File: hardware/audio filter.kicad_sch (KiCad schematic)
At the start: 59 parts, among them J1 721A, J11 Conn_01x09_Pin, J2 35RAPC2AV, J3 35RAPC2AV, J4 35RAPC4BV4, J5 35RAPC2AV, J6 35RAPC4BV4, J7 BPJF04AUX, J8 Conn_01x03_Pin, J9 Conn_01x02_Pin, K1 K1C05, SW2 SW-T2-1C-A-A2-M1, SW3 SW-T2-1C-A-A2-M1, SW4 SW-T2-1C-A-A2-M1, SW5 SW-T2-1C-A-A2-M1, SW6 SW-T2-1C-A-A2-M1, U5 LM4040LP-3

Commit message: Version 0.3 RE-arranged circuit into external connections and on-board headers. Changed FBs to 10uH inductors.
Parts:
- removed FB1, FB2, FB3, FB4, FB5, FB6: FerriteBead, symbol Device:FerriteBead
- removed J11: Conn_01x09_Pin, symbol Connector:Conn_01x09_Pin
- removed J8: Conn_01x03_Pin, symbol Connector:Conn_01x03_Pin
- removed TP1, TP13, TP2, TP3, TP4, TP5: TestPoint, symbol Connector:TestPoint
- added D2: LED, symbol Device:LED
- added J1: Conn_01x13_Pin, symbol Connector:Conn_01x13_Pin
- added J1, J11, J12, J13, J16, J17, J19, J3, J8, J9: Conn_01x01_Socket, symbol Connector:Conn_01x01_Socket
- added J10, J11, J12, J3, J4, J5, J6, J7, J8: Conn_01x02_Pin, symbol Connector:Conn_01x02_Pin
- added J10, J14, J15, J18, J20, J21, J22, J23: Conn_01x02_Socket, symbol Connector:Conn_01x02_Socket
- added J2: Conn_01x04_Pin, symbol Connector:Conn_01x04_Pin
- added L1, L2, L3, L4, L5, L6: 10u, symbol Device:L
- added R1: 470, symbol Device:R
- renumbered J4 to J13, J3 to J14, J5 to J15, J1 to J16, J6 to J17, J7 to J18, SW6 to SW1
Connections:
- net +5V: now also R1.1
- net 3V3: no longer A5.9 (A1), RV2.2
- net DASH: now also J1.12 (Pin_12); no longer C5.1
- net DOT: now also J1.11 (Pin_11); no longer C6.1
- net GND: now also J1.13 (Pin_13), J1.3 (Pin_3), J1.8 (Pin_8), J10.2 (Pin_2), J12.2 (Pin_2), J3.1 (Pin_1), J3.2 (Pin_2), J5.1 (Pin_1), J6.1 (Pin_1), J7.2 (Pin_2); no longer C3.2, C4.2, C5.2, C6.2, C7.2, D4.1 (K), J13.G, J13.S, J14.S, J15.S, J17.G, J17.R, J17.S, J2.S, J2.TN, J9.2 (Pin_2), SW2.1 (A), SW3.1 (A), SW4.1 (A), SW5.1 (A)
- net GNDA: now also J4.1 (Pin_1)
- net KEY_IN: now also J1.10 (Pin_10); no longer C4.1
- net KEY_OUT: now also J2.1 (Pin_1)
- net at D1.2 (A), K1.8, TR2.1 (C): now also J11.2 (Pin_2)
- net at R6.2, TR1.2 (B): now also J5.2 (Pin_2); no longer J17.RN
- net at C1.2, C8.1, R5.1: now also J7.1 (Pin_1); no longer C3.1, J9.1 (Pin_1)
- net at D4.2 (A): now also J23.1 (Pin_1); no longer R8.2
- net at J13.R: now also L4.1
- net at J13.T: now also L5.1
- net AUDIO_IN: now reaches A2.31 (GPIO26_ADC0), C1.1, R3.2, R4.1
- net at SW1.2 (B): now also J20.1 (Pin_1); no longer A1.8 (VIN+)
- net GNDPWR: now reaches C2.2, J16.2
- net GNDPWR: now also C3.2, C4.2, C5.2, C6.2, C7.2, J13.G, J13.S, J14.S, J15.S, J17.G, J17.R, J17.S, J2.S, J2.TN, J10.2 (Pin_2), J14.1 (Pin_1), J20.2 (Pin_2), J21.2 (Pin_2), J22.1 (Pin_1), J3.1 (Pin_1); no longer A1.9 (VIN-)
- net at C2.1, SW1.1 (A): now also L2.2
- net \FC_BW_MODE: now reaches A2.4 (GPIO2), JP1.2 (B)
- net \FC_BW_MODE: now also J1.4 (Pin_4)
- net at SW2.2 (B): now also J1.1 (Pin_1); no longer A2.6 (GPIO4)
- net at A3.7 (LOUT): now also J10.1 (Pin_1); no longer J17.T
- net at J17.TN: now also J22.2 (Pin_2); no longer A4.5 (A+)
- net at C7.1: now also J14.2 (Pin_2), L6.2; no longer K1.6
- net at J2.T: now also L1.1
- net at J18.1 (In): now also J18.1 (Pin_1); no longer A4.7 (Vout+)
- net at J18.2 (Ext): now also J18.2 (Pin_2); no longer A4.6 (Vout-)
- net at SW3.2 (B): now also J8.1 (Pin_1); no longer A2.7 (GPIO5)
- net at BT1.1 (+), J16.1: now also L2.1
- net at J15.T: now also L6.1
- net UART0_TX: now reaches A2.1 (GPIO0)
- net UART0_TX: now also J1.1 (Pin_1)
- net UART0_RX: now reaches A2.2 (GPIO1)
- net UART0_RX: now also J1.2 (Pin_2)
- net SPARE0: now reaches A2.5 (GPIO3)
- net SPARE0: now also J1.5 (Pin_5)
- net at SW4.2 (B): now also J9.1 (Pin_1); no longer A2.9 (GPIO6)
- net at J14.T: now also L3.1
- net LED1 renamed SPARE1
- net SPARE1: now also J2.3 (Pin_3)
- net LED2 renamed SPARE2
- net SPARE2: now also J2.4 (Pin_4)
- net TUNE: no longer names the net of SW5.2 (B)
- net TUNE: now also J11.1 (Pin_1); no longer A2.15 (GPIO11)
- new net: C5.1, J17.1 (Pin_1), L4.2
- new net: C4.1, J13.1 (Pin_1), L3.2
- new net: D4.1 (K), J23.2 (Pin_2)
- new net: J12.1 (Pin_1), R8.2
- new net: A5.9 (A1), RV2.2
- new net: A1.8 (VIN+), J9.1 (Pin_1)
- new net: A1.9 (VIN-), J9.2 (Pin_2)
- new net: J12.1 (Pin_1), SW2.1 (A), SW3.1 (A), SW4.1 (A), SW5.1 (A)
- new net: J17.RN, J17.T, J19.1 (Pin_1), J21.1 (Pin_1)
- new net: J11.1 (Pin_1), R1.2
- new net: J6.2 (Pin_2), K1.6
- new net: D2.1 (K), J15.2 (Pin_2)
- new net: D2.2 (A), J15.1 (Pin_1)
- new net: C3.1, J10.1 (Pin_1), L1.2
- new net: A4.7 (Vout+), J8.1 (Pin_1)
- new net: A4.6 (Vout-), J8.2 (Pin_2)
- new net: C6.1, J16.1 (Pin_1), L5.2
- new net: A4.5 (A+), J4.2 (Pin_2)
- new net \ALE_IN: A2.7 (GPIO5), J1.7 (Pin_7)
- new net \AN: A2.9 (GPIO6), J1.9 (Pin_9)
- new net \FILTER_IN: A2.6 (GPIO4), J1.6 (Pin_6)
- new net \TUNE: A2.15 (GPIO11), J2.2 (Pin_2)
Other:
- note added: "1 S"
- note added: "2 T"
- note added: "3 RN"
- note added: "35RAPC4BV4"
- note added: "4 R"
- note added: "5 TN"
- note added: "G"
- note added: "Isolate from Ground"
- note added: "TUNE LED RED, 3mm"
- note removed: "Debugger"
- moved on the sheet: A1, A2, A3, A4, A5, BT1, C1, D1, D4, J13, J14, J15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

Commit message: Revision A (Prototype).
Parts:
- removed J19: Conn_01x01_Socket, symbol Connector:Conn_01x01_Socket
- removed J2: Conn_01x04_Pin, symbol Connector:Conn_01x04_Pin
- added PL2: Conn_01x04_Pin, symbol Connector:Conn_01x04_Pin
- added SK5: Conn_01x02_Socket, symbol Connector:Conn_01x02_Socket
- renumbered J13 to J1, J14 to J2, J15 to J3, J2 to J4, J16 to J5, J17 to J6, J18 to J7, J1 to PL1, J10 to PL10, J11 to PL11, J12 to PL12, J3 to PL3, J4 to PL4, J5 to PL5, J6 to PL6, J7 to PL7, J8 to PL8, J9 to PL9, J21 to SK10, J15 to SK11, J23 to SK12, J1 to SK1a1, J8 to SK1b1, J12 to SK1c1, J9 to SK1d1, J13 to SK1e1, J16 to SK1f1, J17 to SK1g1, J3 to SK1h1, J11 to SK2a1, J22 to SK4, J14 to SK6, J10 to SK7, J18 to SK8, J20 to SK9
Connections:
- net KEY_OUT: now also PL2.1 (Pin_1)
- net SPARE1: now also PL2.3 (Pin_3)
- net SPARE2: now also PL2.4 (Pin_4)
- net \TUNE: now also PL2.2 (Pin_2)
- net at J6.RN, J6.T, SK10.1 (Pin_1): now also SK5.2 (Pin_2)

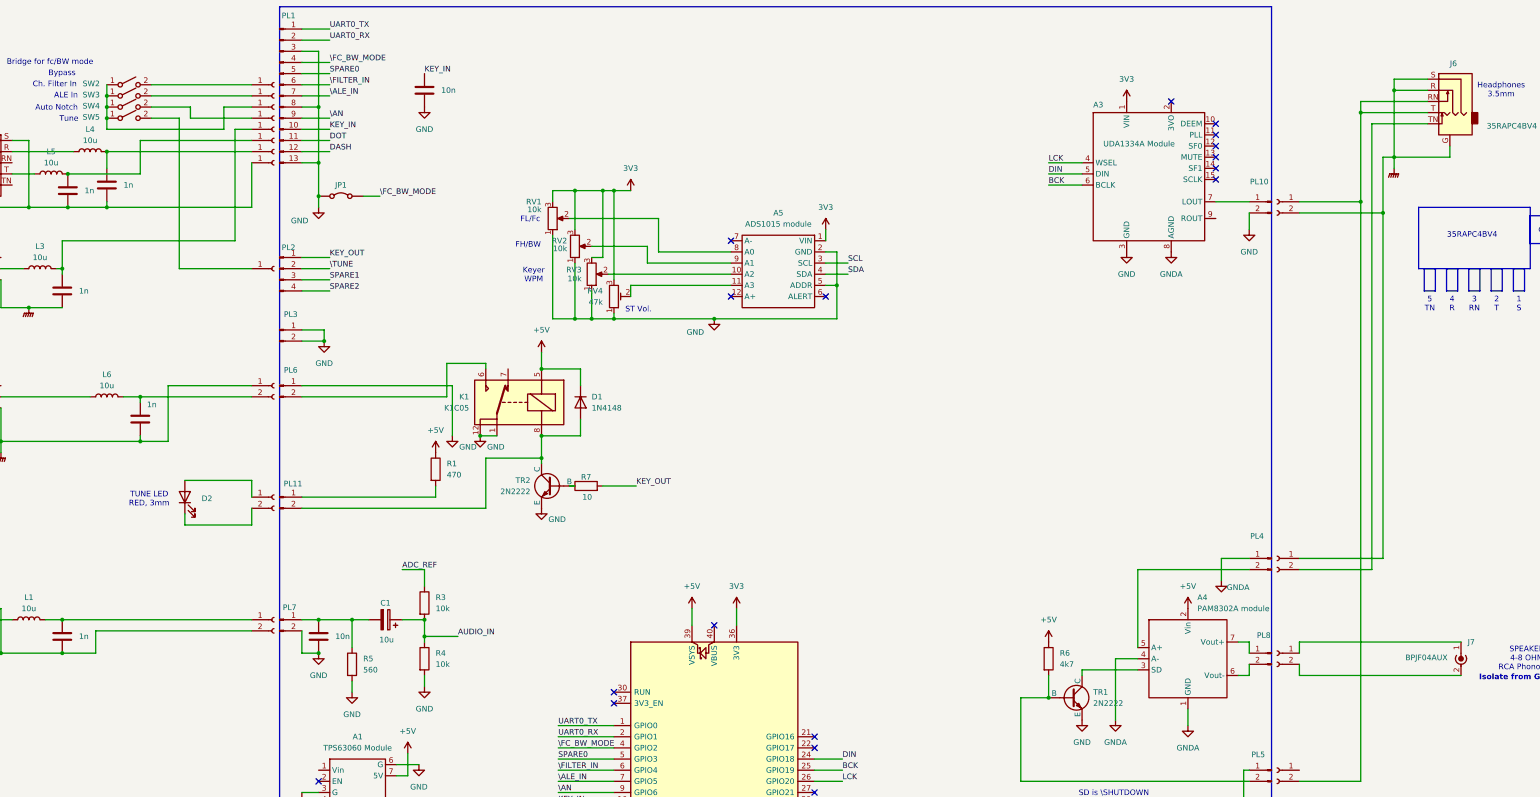
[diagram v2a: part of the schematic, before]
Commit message: Added 1n C10/C11 to SPKR output to filter out RF. Started modle footprint library.
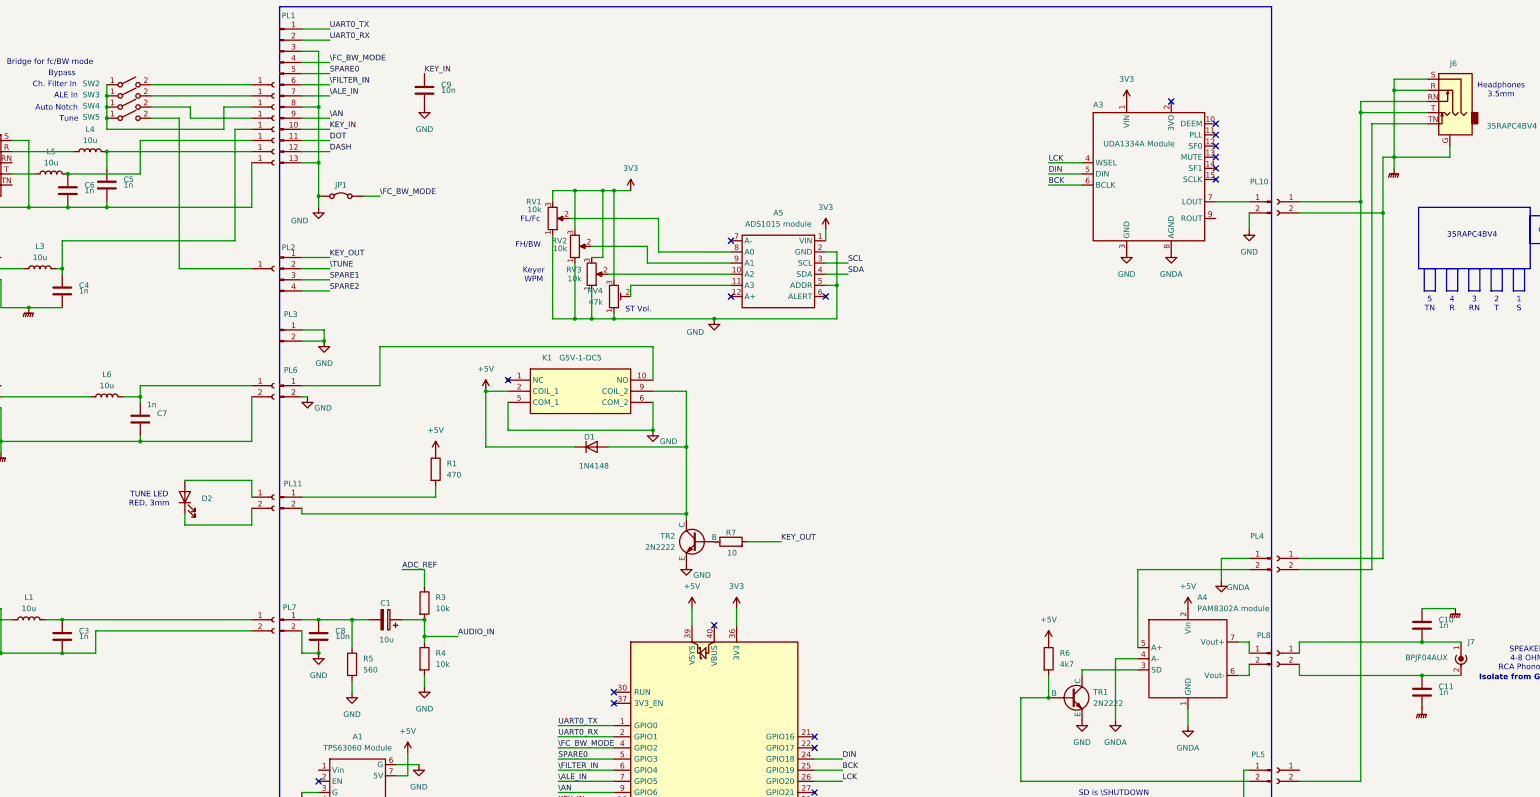
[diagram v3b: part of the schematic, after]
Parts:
- removed K1: K1C05, symbol Project_Library:K1C05
- added C10, C11: 1n, symbol Device:C
- added K1: G5V-1-DC5, Project_Library:G5V1DC5, symbol Project_Library:G5V-1-DC5
- C1: footprint (none) -> Capacitor_THT:CP_Radial_D5.0mm_P2.50mm
- C8, C9: footprint (none) -> Capacitor_THT:C_Rect_L4.0mm_W2.5mm_P2.50mm
- D1: footprint Diode_SMD:D_SOD-523 -> Diode_THT:D_DO-15_P2.54mm_Vertical_KathodeUp
- D2, D4: footprint (none) -> LED_THT:LED_D3.0mm
- JP1: footprint (none) -> Jumper:Jumper_Harwin_S1621_P10.9mm
- PL1: footprint (none) -> Connector_PinHeader_2.54mm:PinHeader_1x13_P2.54mm_Vertical
- PL10, PL11, PL12, PL3, PL4, PL5, PL6, PL7, PL8, PL9: footprint (none) -> Connector_PinHeader_2.54mm:PinHeader_1x02_P2.54mm_Vertical
- PL2: footprint (none) -> Connector_PinHeader_2.54mm:PinHeader_1x04_P2.54mm_Vertical
- R1, R3, R4, R5, R6, R7, R8: footprint (none) -> Resistor_THT:R_Axial_DIN0207_L6.3mm_D2.5mm_P10.16mm_Horizontal
- RV1, RV2, RV3: footprint (none) -> Potentiometer_THT:Potentiometer_Alps_RK09K_Single_Vertical
- RV4: footprint (none) -> Potentiometer_THT:Potentiometer_Piher_PT-10-H05_Horizontal
- TR1, TR2: footprint (none) -> Package_TO_SOT_THT:TO-92
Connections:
- net +5V: now also K1.2 (COIL_1)
- net GND: now also PL6.2 (Pin_2), K1.5 (COM_1), K1.6 (COM_2); no longer PL6.1 (Pin_1)
- net GNDPWR: now also SK6.2 (Pin_2), C10.1, C11.2; no longer SK6.1 (Pin_1)
- net at D1.2 (A), PL11.2 (Pin_2), TR2.1 (C): now also K1.9 (COIL_2)
- net at C7.1, L6.2: now also SK6.1 (Pin_1); no longer SK6.2 (Pin_2)
- net at J7.1 (In), SK8.1 (Pin_1): now also C10.2
- net at J7.2 (Ext), SK8.2 (Pin_2): now also C11.1
- new net: K1.10 (NO), PL6.1 (Pin_1)
- no-connect marks 22 -> 23
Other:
- moved on the sheet: D1, R7, TR2

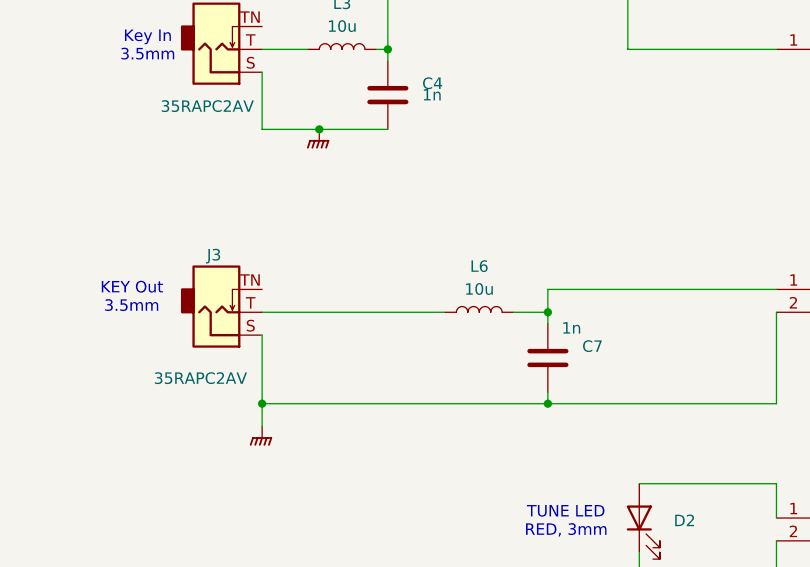
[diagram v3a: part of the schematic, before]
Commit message: Removed the 10uH choke from Key out.
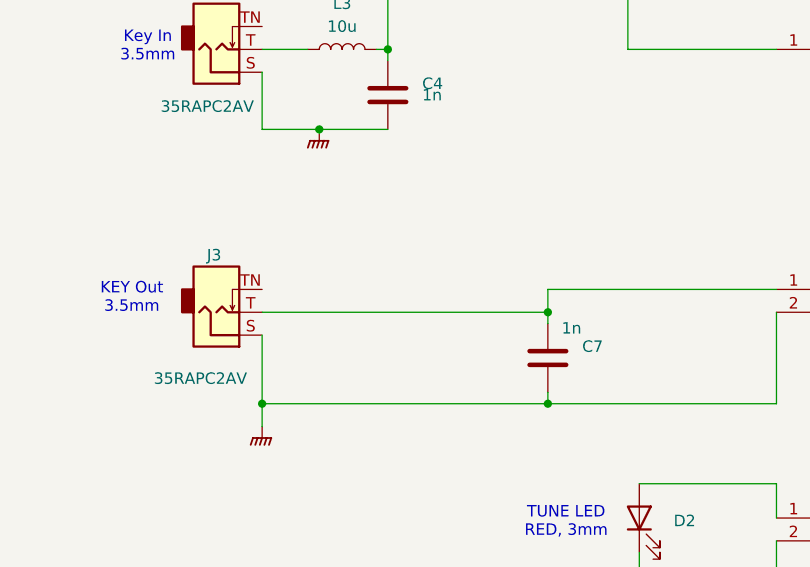
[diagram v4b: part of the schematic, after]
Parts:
- removed L6: 10u, symbol Device:L
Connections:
- net at J3.T: now also C7.1, SK6.1 (Pin_1)
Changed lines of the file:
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@@
 	(title_block
 		(title "DSP Audio Filter")
-		(date "2025-10-15")
-		(rev "|A")
+		(date "2025-12-23")
+		(rev "A.5")
 		(company "Adrian Nash, G4ZHZ")
 	)
@@
 	(wire
 		(pts
-			(xy 40.64 107.95) (xy 60.96 107.95)
+			(xy 40.64 107.95) (xy 72.39 107.95)
 		)
 		(stroke
@@
 	(wire
 		(pts
-			(xy 68.58 107.95) (xy 72.39 107.95)
-		)
-		(stroke
-			(width 0)
-			(type default)
-		)
-	)
-	(wire
-		(pts
 			(xy 113.03 62.23) (xy 113.03 64.77)
 		)
@@
 					(unit 1)
 				)
-			)
-		)
-	)
-	(symbol
-		(lib_id "Device:L")
-		(at 64.77 107.95 90)
-		(unit 1)
-		(exclude_from_sim no)
-		(in_bom yes)
-		(on_board no)
-		(dnp no)
-		(fields_autoplaced yes)
-		(property "Reference" "L6"
-			(at 64.77 102.87 90)
-			(effects
-				(font
-					(size 1.27 1.27)
-				)
-			)
-		)
-		(property "Value" "10u"
-			(at 64.77 105.41 90)
-			(effects
-				(font
-					(size 1.27 1.27)
-				)
-			)
-		)
-		(property "Footprint" ""
-			(at 64.77 107.95 0)
-			(effects
-				(font
-					(size 1.27 1.27)
-				)
-				(hide yes)
-			)
-		)
-		(property "Datasheet" "~"
-			(at 64.77 107.95 0)
-			(effects
-				(font
-					(size 1.27 1.27)
-				)
-				(hide yes)
-			)
-		)
-		(property "Description" "Inductor"
-			(at 64.77 107.95 0)
-			(effects
-				(font
-					(size 1.27 1.27)
-				)
-				(hide yes)
-			)
-		)
-		(pin "2"
-		)
-		(pin "1"
-		)
-		(instances
-			(project "audio filter"
-				(path "/07ca0058-fccf-4127-8cf6-d53d8308f6c1"
-					(reference "L6")
-					(unit 1)
-				)
